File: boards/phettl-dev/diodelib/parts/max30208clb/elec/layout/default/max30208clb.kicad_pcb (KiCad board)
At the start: 4 copper layers, 2 parts, among them U1 ?

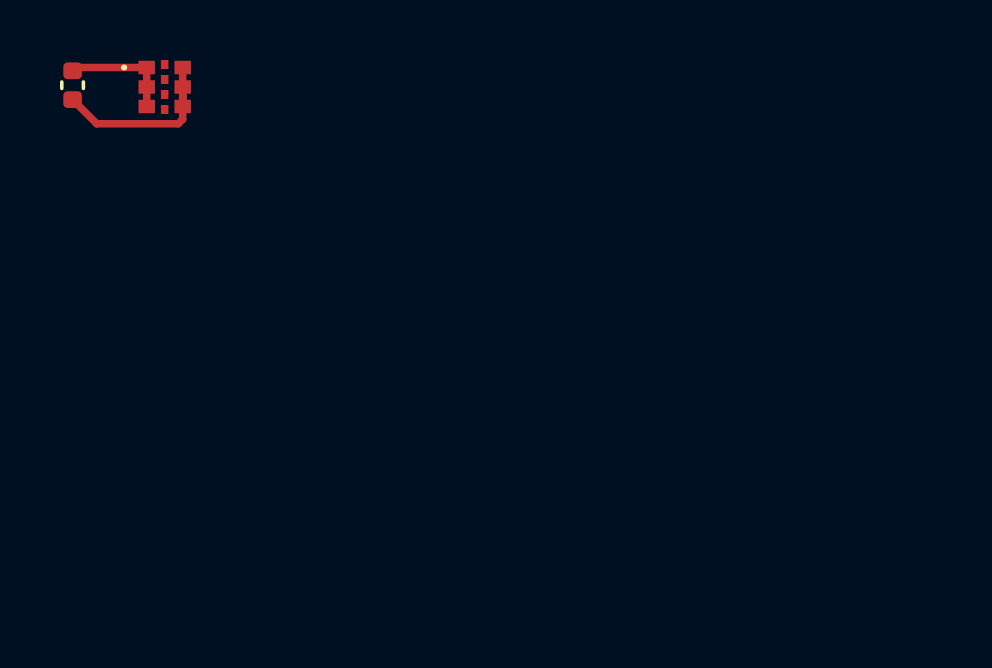
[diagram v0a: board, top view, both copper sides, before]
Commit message: [PART] add temp sensor
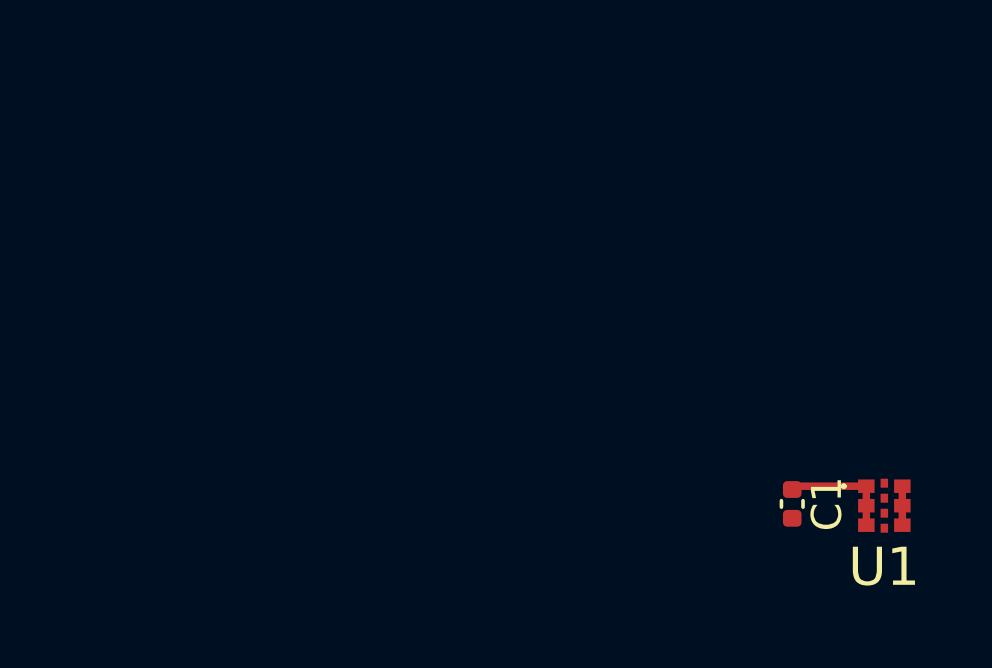
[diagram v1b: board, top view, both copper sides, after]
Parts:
- moved C1 27.8 mm to (153.4, 102.8)
- moved U1 27.8 mm to (156.5, 102.8)
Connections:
- net temp-gnd renamed gnd
- net temp-io renamed io
- net temp-io-1 renamed io-1
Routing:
- net gnd: track 6.44 -> 1.30 mm
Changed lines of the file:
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@@
 	(layers
 		(0 "F.Cu" signal)
-		(1 "In1.Cu" power)
-		(2 "In2.Cu" mixed)
+		(1 "In1.Cu" signal)
+		(2 "In2.Cu" signal)
 		(31 "B.Cu" signal)
 		(32 "B.Adhes" user "B.Adhesive")
@@
 	)
 	(net 0 "")
-	(net 1 "sda")
-	(net 2 "temp-gnd")
-	(net 3 "scl")
-	(net 4 "temp-io")
-	(net 5 "temp-io-1")
-	(net 6 "vcc")
+	(net 1 "scl")
+	(net 2 "vcc")
+	(net 3 "io-1")
+	(net 4 "gnd")
+	(net 5 "sda")
+	(net 6 "io")
 	(footprint "lib:MAX30208CLBT"
 		(layer "F.Cu")
-		(at 132.522096 88.863374)
+		(at 156.51 102.82)
 		(descr "MAX30208CLB+T-3")
 		(tags "Integrated Circuit")
 		(property "Reference" "U1"
-			(at -0.01 2.05 360)
+			(at -0.01 2.05 0)
+			(layer "F.SilkS")
+			(effects
+				(font
+					(size 1.27 1.27)
+					(thickness 0.254)
+				)
+			)
+		)
+		(property "Value" "?"
+			(at -0.2 0 0)
 			(layer "F.SilkS")
 			(hide yes)
@@
 			)
 		)
-		(property "Value" "?"
-			(at -0.2 0 360)
-			(layer "F.SilkS")
+		(property "Footprint" ""
+			(at 0 0 0)
+			(layer "F.Fab")
 			(hide yes)
 			(effects
 				(font
 					(size 1.27 1.27)
-					(thickness 0.254)
-				)
-			)
-		)
-		(property "Footprint" ""
-			(at 0 0 360)
+					(thickness 0.15)
+				)
+			)
+		)
+		(property "Datasheet" ""
+			(at 0 0 0)
 			(layer "F.Fab")
 			(hide yes)
@@
 			)
 		)
-		(property "Datasheet" ""
-			(at 0 0 360)
-			(layer "F.Fab")
-			(hide yes)
-			(effects
-				(font
-					(size 1.27 1.27)
-					(thickness 0.15)
-				)
-			)
-		)
 		(property "Description" ""
-			(at 0 0 360)
+			(at 0 0 0)
 			(layer "F.Fab")
 			(hide yes)
@@
 		)
 		(fp_text user "${REFERENCE}"
-			(at -0.2 0 360)
+			(at 0.01 -1.9 0)
 			(layer "F.Fab")
 			(effects
@@
 			(size 0.45 0.55)
 			(layers "F.Cu" "F.Paste" "F.Mask")
-			(net 6 "vcc")
+			(net 2 "vcc")
 			(pintype "stereo")
 		)
@@
 			(size 0.45 0.55)
 			(layers "F.Cu" "F.Paste" "F.Mask")
-			(net 6 "vcc")
+			(net 2 "vcc")
 			(pintype "stereo")
 		)
@@
 			(size 0.45 0.55)
 			(layers "F.Cu" "F.Paste" "F.Mask")
-			(net 6 "vcc")
+			(net 2 "vcc")
 			(pintype "stereo")
 		)
@@
 			(size 0.45 0.55)
 			(layers "F.Cu" "F.Paste" "F.Mask")
-			(net 2 "temp-gnd")
+			(net 4 "gnd")
 			(pintype "stereo")
 		)
@@
 			(size 0.45 0.55)
 			(layers "F.Cu" "F.Paste" "F.Mask")
-			(net 2 "temp-gnd")
+			(net 4 "gnd")
 			(pintype "stereo")
 		)
@@
 			(size 0.45 0.55)
 			(layers "F.Cu" "F.Paste" "F.Mask")
-			(net 2 "temp-gnd")
+			(net 4 "gnd")
 			(pintype "stereo")
 		)
@@
 			(size 0.25 0.3)
 			(layers "F.Cu" "F.Paste" "F.Mask")
-			(net 4 "temp-io")
+			(net 6 "io")
 			(pintype "stereo")
 		)
@@
 			(size 0.25 0.3)
 			(layers "F.Cu" "F.Paste" "F.Mask")
-			(net 1 "sda")
+			(net 5 "sda")
 			(pintype "stereo")
 		)
@@
 			(size 0.25 0.3)
 			(layers "F.Cu" "F.Paste" "F.Mask")
-			(net 3 "scl")
+			(net 1 "scl")
 			(pintype "stereo")
 		)
@@
 			(size 0.25 0.3)
 			(layers "F.Cu" "F.Paste" "F.Mask")
-			(net 5 "temp-io-1")
+			(net 3 "io-1")
 			(pintype "stereo")
 		)
@@
 	(footprint "lib:C0402"
 		(layer "F.Cu")
-		(at 129.452096 88.803374 -90)
+		(at 153.44 102.76 -90)
 		(descr "Capacitor SMD 0402 (1005 Metric), square (rectangular) end terminal, IPC_7351 nominal, (Body size source: IPC-SM-782 page 76, https://www.pcb-3d.com/wordpress/wp-content/uploads/ipc-sm-782a_amendment_1_and_2.pdf), generated with kicad-footprint-generator")
 		(tags "capacitor")
@@
 			(at 0 -1.16 90)
 			(layer "F.SilkS")
-			(hide yes)
 			(effects
 				(font
@@
 			(layers "F.Cu" "F.Paste" "F.Mask")
 			(roundrect_rratio 0.25)
-			(net 6 "vcc")
+			(net 2 "vcc")
 			(pintype "stereo")
 		)
@@
 			(layers "F.Cu" "F.Paste" "F.Mask")
 			(roundrect_rratio 0.25)
-			(net 2 "temp-gnd")
+			(net 4 "gnd")
 			(pintype "stereo")
 		)
@@
 	)
 	(segment
-		(start 133.122096 89.938374)
-		(end 133.122096 88.863374)
+		(start 153.55 102.17)
+		(end 153.44 102.28)
 		(width 0.25)
 		(layer "F.Cu")
@@
 	)
 	(segment
-		(start 129.452096 89.283374)
-		(end 130.257096 90.088374)
+		(start 155.91 102.17)
+		(end 155.91 103.47)
 		(width 0.25)
 		(layer "F.Cu")
@@
 	)
 	(segment
-		(start 132.972096 90.088374)
-		(end 133.122096 89.938374)
+		(start 155.91 102.17)
+		(end 153.55 102.17)
 		(width 0.25)
 		(layer "F.Cu")
@@
 	)
 	(segment
-		(start 130.257096 90.088374)
-		(end 132.972096 90.088374)
+		(start 157.11 102.17)
+		(end 157.11 103.47)
 		(width 0.25)
 		(layer "F.Cu")
-		(net 2)
-	)
-	(segment
-		(start 133.122096 88.213374)
-		(end 133.122096 89.513374)
-		(width 0.25)
-		(layer "F.Cu")
-		(net 2)
-	)
-	(segment
-		(start 131.922096 88.213374)
-		(end 129.562096 88.213374)
-		(width 0.25)
-		(layer "F.Cu")
-		(net 6)
-	)
-	(segment
-		(start 131.922096 88.213374)
-		(end 131.922096 89.513374)
-		(width 0.25)
-		(layer "F.Cu")
-		(net 6)
-	)
-	(segment
-		(start 129.562096 88.213374)
-		(end 129.452096 88.323374)
-		(width 0.25)
-		(layer "F.Cu")
-		(net 6)
-	)
-	(group "temp"
-		(members "54f6942b-133e-431d-8f3e-dfd963929099" "5723da48-4ac6-40a0-9f4a-124c041dd93a"
-			"a6cdf26a-6230-46b7-9579-e04c667e1c0b" "cd57f018-24e7-4f83-82fa-a2a8f9197c95"
-			"db990f9d-dc53-46df-b6d8-997be95b75b2" "fc3fba07-bc57-4ea7-82c7-29f78c51bfce"
-		)
+		(net 4)
 	)
 )
